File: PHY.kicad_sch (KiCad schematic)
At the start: 1 part

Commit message: wired phy controller
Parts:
- removed PHY_Interface?: KSZ8721BT, TQFP48_7x7MC_MCH, symbol local_library:KSZ8721BT
- added C? (x3): 3.3uF, symbol Device:C_Polarized
- added C? (x2): 27pf, symbol Device:C
- added C? (x9): 0.1uF, symbol Device:C
- added C?: 10uF, symbol Device:C_Polarized
- added D? (x2): LED, symbol Device:LED
- added FB? (x3): FerriteBead, symbol Device:FerriteBead
- added JP? (x4): SolderJumper_2_Open, symbol Jumper:SolderJumper_2_Open
- added R? (x11): 49.9, symbol Device:R
- added R?: 12.4k, symbol Device:R
- added R? (x4): 56.2, symbol Device:R
- added R? (x2): 10k, symbol Device:R
- added R? (x4): 332, symbol Device:R
- added R?: 63.4, symbol Device:R
- added R?: 1M, symbol Device:R
- added TP?: TestPoint, symbol Connector:TestPoint
- added U?: LAN83C185-JT, TQFP64_10x10MC_MCH, symbol 2023-02-27_15-58-55:LAN83C185-JT
- added Y?: 25 MHz, symbol Device:Crystal
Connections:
- new net: R?.1, U?.48 (CRS)
- new net: R?.1, U?.59 (EXRES1)
- new net: JP?.1 (A), R?.2 (x4)
- new net: TP?.1, U?.46 (NINT)
- new net: R?.2, U?.25 (NRST)
- new net: R?.2, U?.26 (MDIO)
- new net: D?.1 (K), R?.1 (x2)
- new net: R?.1, U?.34 (RX_CLK)
- new net: C?.1, R?.2, U?.23 (CLKIN/XTAL1), Y?.2
- new net: R?.2, U?.30 (RXD2)
- new net: R?.2, U?.11 (CLK_FREQ)
- new net: JP?.2 (B), U?.6 (MODE2)
- new net: JP?.2 (B), U?.4 (MODE0)
- new net: JP?.2 (B), U?.5 (MODE1)
- new net: R?.1, U?.35 (RX_ER/RXD4)
- new net: C?.1, R?.1, R?.1, Y?.1
- new net: R?.2, U?.22 (XTAL2)
- new net: R?.2, U?.32 (RXD0)
- new net: R?.2, U?.29 (RXD3)
- new net: JP?.2 (B), U?.2 (GPO1/PHYAD4)
- new net: R?.1, U?.47 (COL)
- new net: R?.2, U?.31 (RXD1)
- new net: R?.1, U?.33 (RX_DV)
- new net: R?.1, U?.38 (TX_CLK)
- new net +3V3: C?.1, FB?.1, FB?.1, FB?.1, R?.1
- new net ETH-L1N: R?.1
- new net ETH-L1P: D?.2 (A), D?.2 (A), U?.16 (SPEED100/PHYAD0)
- new net ETH-L2N: R?.1
- new net GND: C?.2, C?.2, C?.2, C?.2, C?.2, C?.2, C?.2, C?.2, C?.2, C?.2, C?.2, C?.2, C?.2, C?.2, C?.2, R?.1, R?.1, R?.1, R?.1, R?.1, R?.2, R?.2, R?.2, R?.2, R?.2
- new net MAG-RXn: U?.54 (RXN)
- new net MAG-RXp: U?.55 (RXP)
- new net MAG-TXn: U?.50 (TXN)
- new net MAG-TXp: U?.51 (TXP)
- new net PHY-AD1: U?.17 (LINKON/PHYAD1)
- new net PHY-AD2: U?.19 (ACTIVITY/PHYAD2)
- new net PHY-AD3: U?.20 (FDUPLE/PHYAD3)
- new net PHY-AVDD: C?.1, C?.1, C?.1, C?.1, C?.1, FB?.2, U?.53 (AVDD1), U?.57 (AVDD2), U?.61 (AVDD3), U?.63 (AVDD4)
- new net PHY-AVSS: U?.49 (AVSS1), U?.52 (AVSS2), U?.58 (AVSS3), U?.60 (AVSS4), U?.62 (AVSS5)
- new net PHY-COL: R?.2
- new net PHY-CRS: R?.2
- new net PHY-MCD: U?.27 (MDC)
- new net PHY-MDIO: R?.1
- new net PHY-RXD0: R?.1
- new net PHY-RXD1: R?.1
- new net PHY-RXD2: R?.1
- new net PHY-RXD3: R?.1
- new net PHY-RX_CLK: R?.2
- new net PHY-RX_DV: R?.2
- new net PHY-RX_ER: R?.2
- new net PHY-TXD0: U?.41 (TXD0)
- new net PHY-TXD1: U?.42 (TXD1)
- new net PHY-TXD2: U?.44 (TXD2)
- new net PHY-TXD3: U?.45 (TXD3)
- new net PHY-TX_CLK: R?.2
- new net PHY-TX_EN: U?.39 (TX_EN)
- new net PHY-TX_ER: U?.37 (TX_ER/TXD4)
- new net PHY-VDD: C?.1, C?.1, C?.1, C?.1, FB?.2, U?.12 (REG_EN), U?.18 (VDD2), U?.43 (VDD3), U?.8 (VDD1)
- new net PHY-VDD-CORE: C?.1, U?.14 (VDD_CORE)
- new net PHY-VREG: C?.1, C?.1, FB?.2, U?.13 (VREG)
- new net PHY-VSS: U?.15 (VSS2), U?.21 (VSS3), U?.24 (VSS4), U?.28 (VSS5), U?.36 (VSS6), U?.40 (VSS7), U?.7 (VSS1)
- no-connect marks 0 -> 4

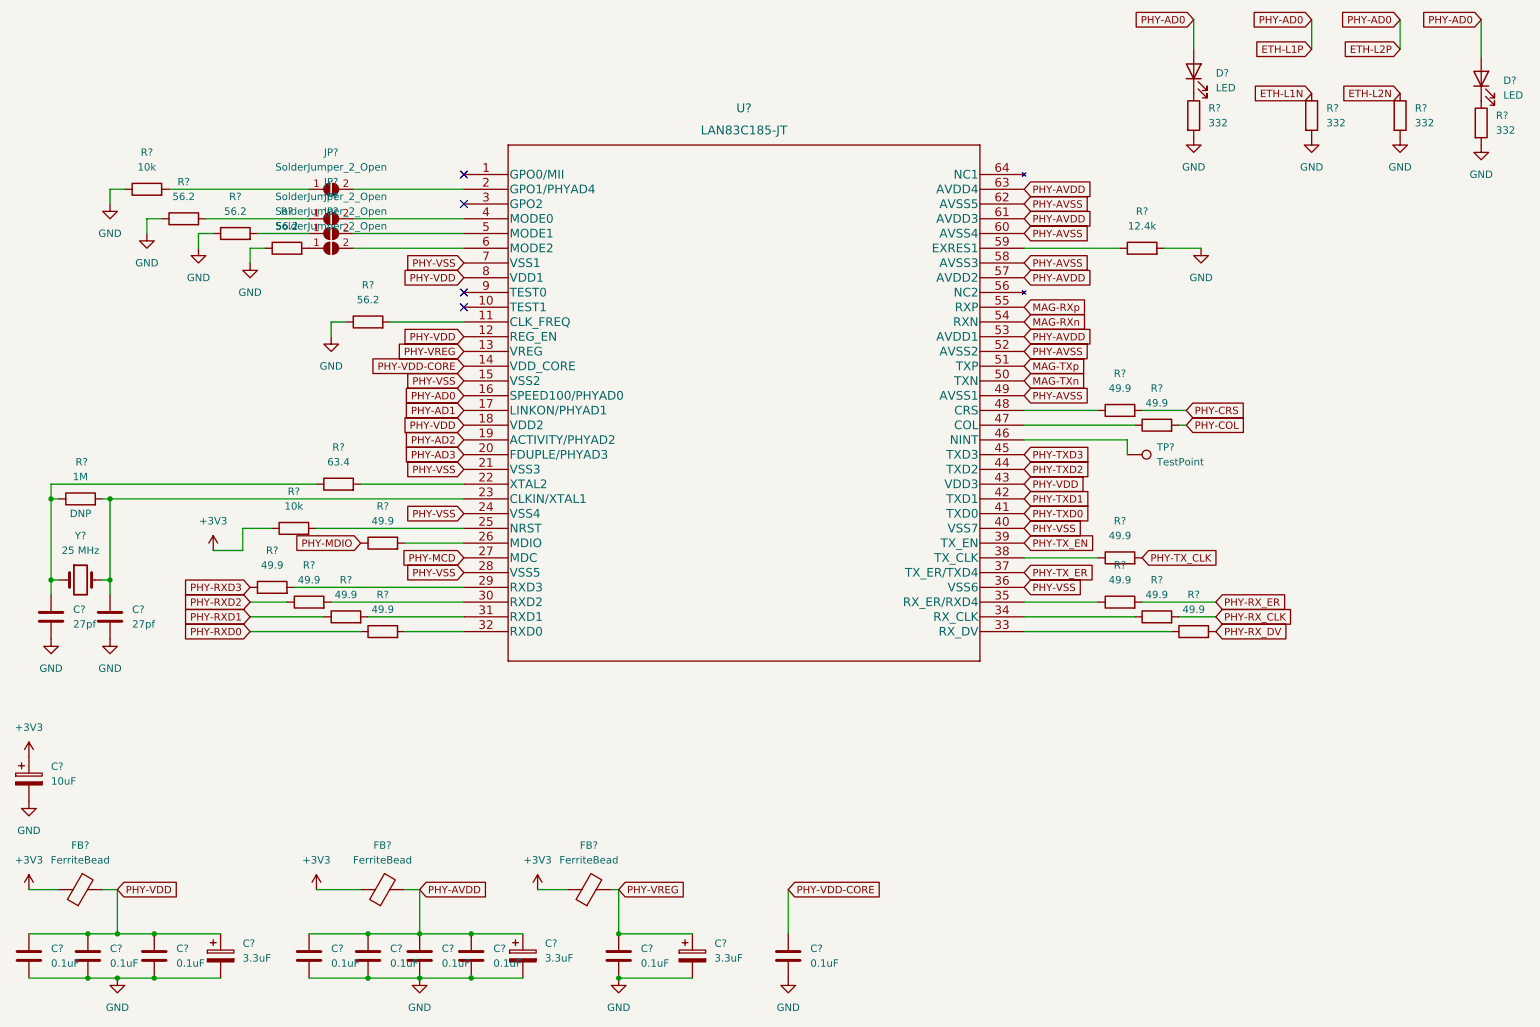
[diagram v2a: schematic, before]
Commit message: add component numbers to schematic
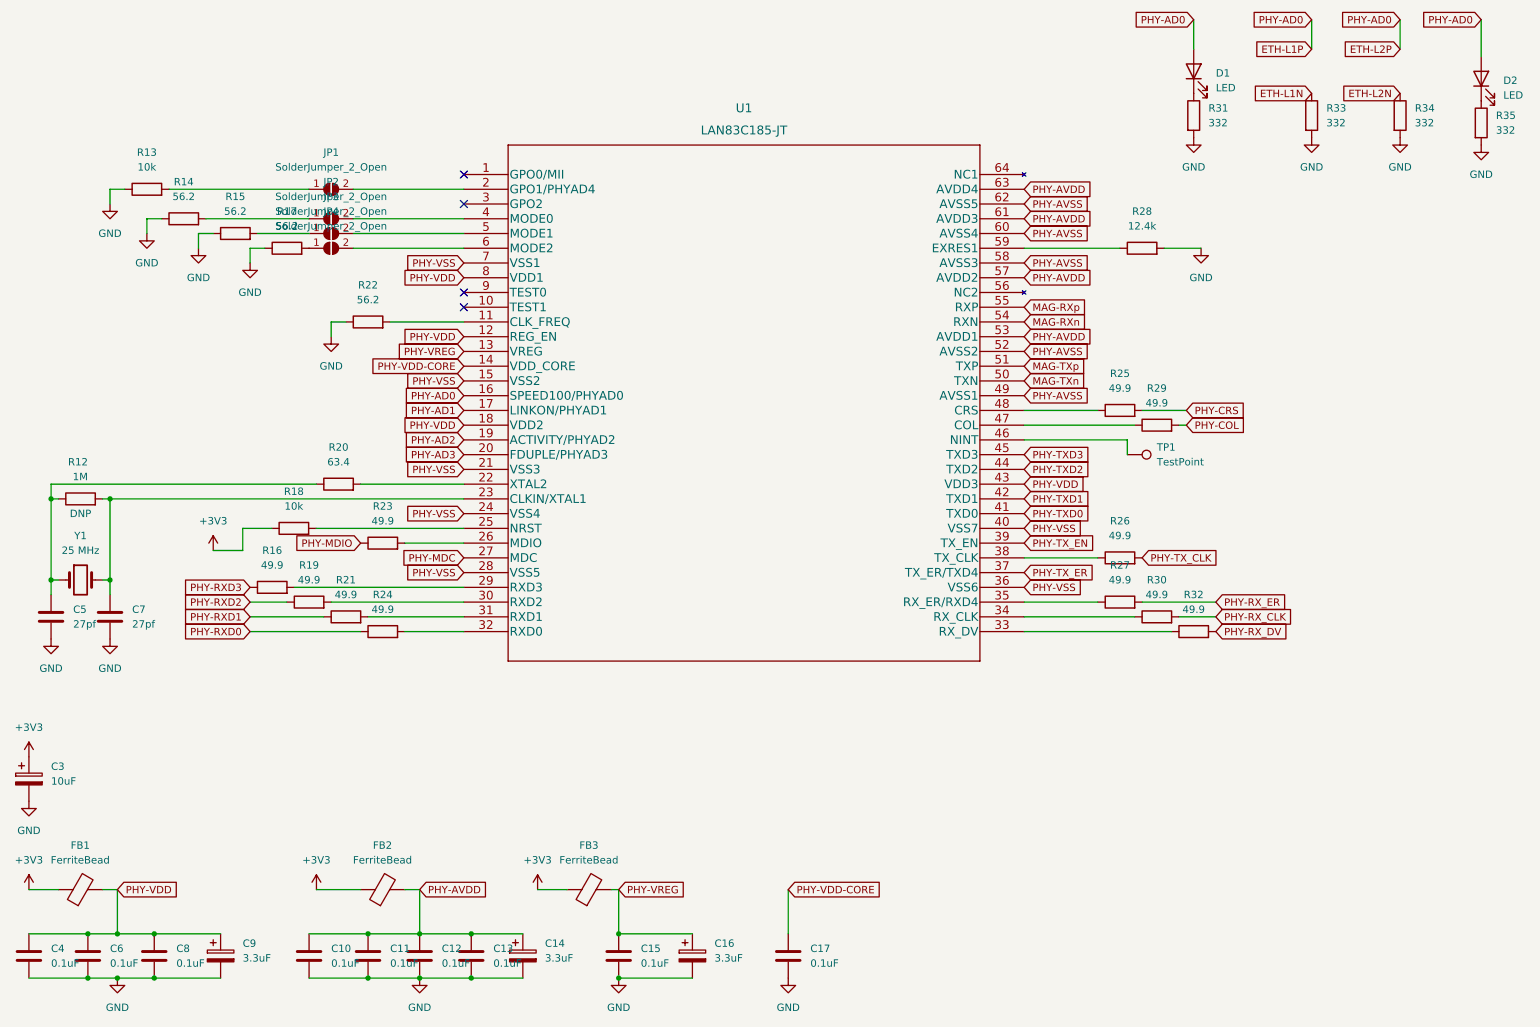
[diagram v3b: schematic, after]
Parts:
- gave numbers to parts that had none: 51
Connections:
- net PHY-MCD renamed PHY-MDC

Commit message: fix nets and wire FPGA
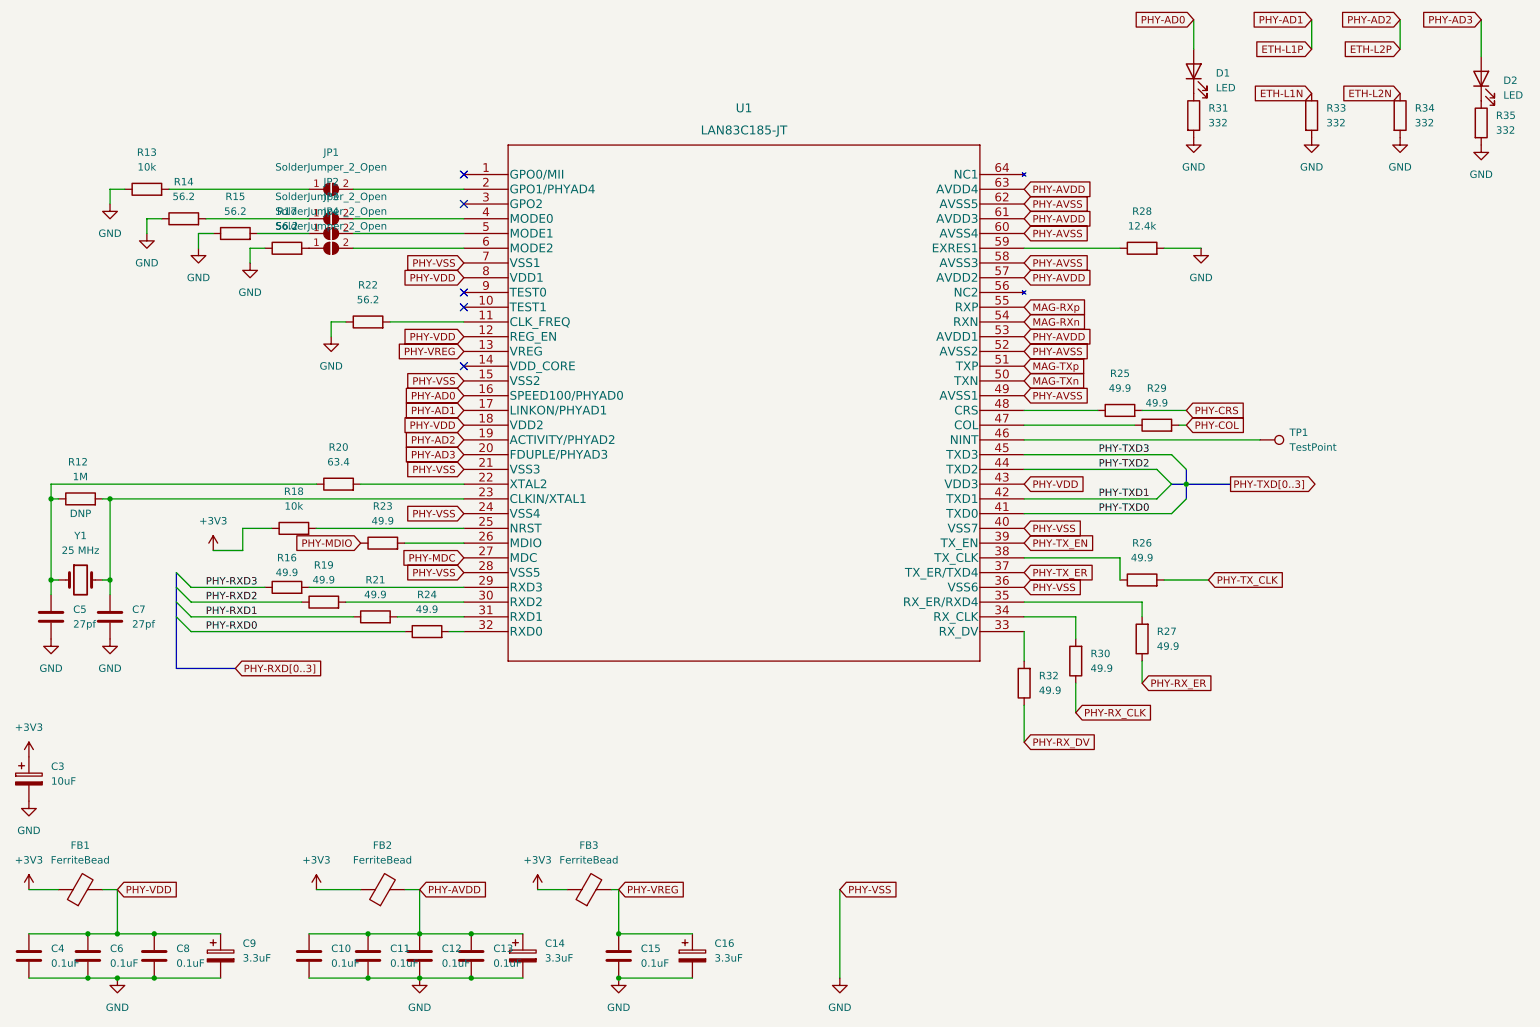
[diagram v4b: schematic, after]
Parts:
- removed C17: 0.1uF, symbol Device:C
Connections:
- net PHY-AD1 is gone; now on net ETH-L1P: U1.17 (LINKON/PHYAD1)
- net PHY-VSS is gone; now on net GND: U1.15 (VSS2), U1.21 (VSS3), U1.24 (VSS4), U1.28 (VSS5), U1.36 (VSS6), U1.40 (VSS7), U1.7 (VSS1)
- net ETH-L1P: no longer D1.2 (A), D2.2 (A), U1.16 (SPEED100/PHYAD0)
- net PHY-AD3: now also D2.2 (A)
- net PHY-RX_CLK: now also R30.1; no longer R30.2
- net PHY-RX_DV: now also R32.1; no longer R32.2
- net PHY-RX_ER: now also R27.1; no longer R27.2
- net at U1.34 (RX_CLK): now also R30.2; no longer R30.1
- net at U1.35 (RX_ER/RXD4): now also R27.2; no longer R27.1
- net at U1.33 (RX_DV): now also R32.2; no longer R32.1
- net PHY-AD2 renamed ETH-L2P
- net PHY-VDD-CORE: no longer names the net of U1.14 (VDD_CORE)
- new net PHY-AD0: D1.2 (A), U1.16 (SPEED100/PHYAD0)
- no-connect marks 4 -> 5
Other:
- moved on the sheet: R16, R19, R21, R24, R26, R27, R30, R32, TP1

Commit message: Assign footprints to ICs
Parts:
- U1: footprint TQFP64_10x10MC_MCH -> Package_QFP:TQFP-64_10x10mm_P0.5mm
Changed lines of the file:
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@@
       (effects (font (size 1.524 1.524)))
     )
-    (property "Footprint" "TQFP64_10x10MC_MCH" (id 2) (at 142.24 43.434 0)
+    (property "Footprint" "Package_QFP:TQFP-64_10x10mm_P0.5mm" (id 2) (at 142.24 43.434 0)
       (effects (font (size 1.524 1.524)) hide)
     )

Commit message: Resistor and cap footprints (except the ones the store cupboard doesn't have)
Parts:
- C10, C11, C12, C13, C15, C4, C6, C8: footprint (none) -> Capacitor_SMD:C_0805_2012Metric_Pad1.18x1.45mm_HandSolder
- C14, C16, C9: footprint (none) -> Capacitor_Tantalum_SMD:CP_EIA-6032-15_Kemet-U_Pad2.25x2.35mm_HandSolder
- C3: footprint (none) -> Capacitor_Tantalum_SMD:CP_EIA-7343-15_Kemet-W_Pad2.25x2.55mm_HandSolder
- R12, R13, R14, R15, R16, R17, R18, R19, R20, R21, R22, R23, R24, R25, R26, R27, R28, R29, R30, R31, R32, R33, R34, R35: footprint (none) -> Resistor_SMD:R_0805_2012Metric_Pad1.20x1.40mm_HandSolder
